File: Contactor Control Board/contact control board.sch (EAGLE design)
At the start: 36 parts, among them Q1 2n2222, Q2 2n2222, Q3 2n2222, Q4 MOSFET-NCHANNELFQP30N06L

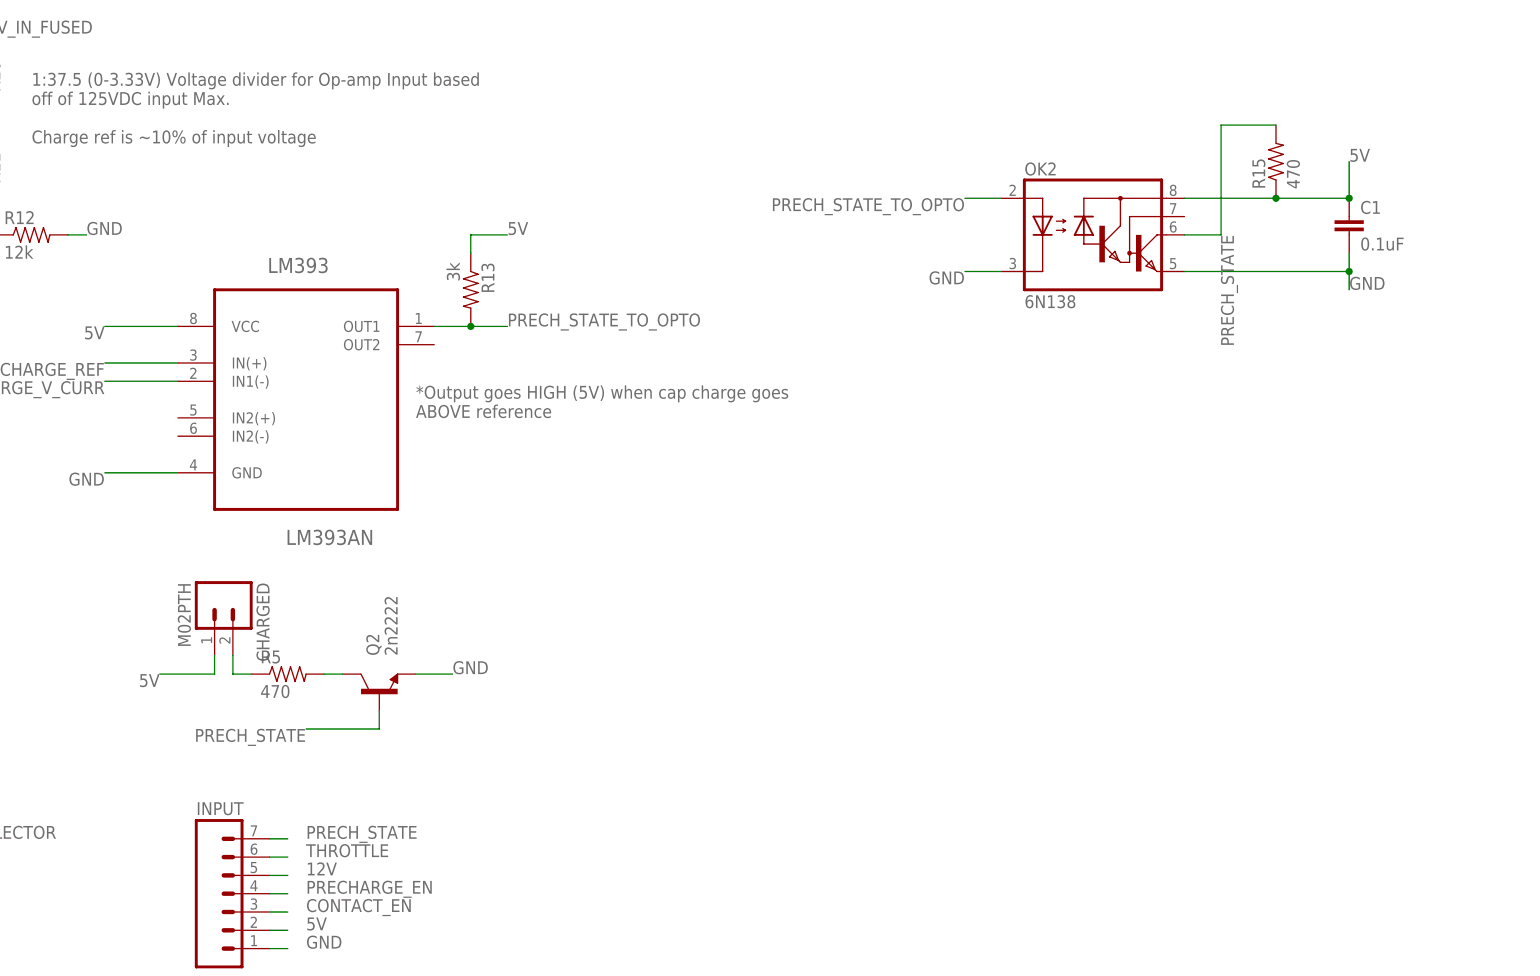
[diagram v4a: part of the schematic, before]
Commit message: Added buffer to use the output of the Op-Amp and split
it between an indicator LED and a digital signal output. Tested and
validated using breadboards
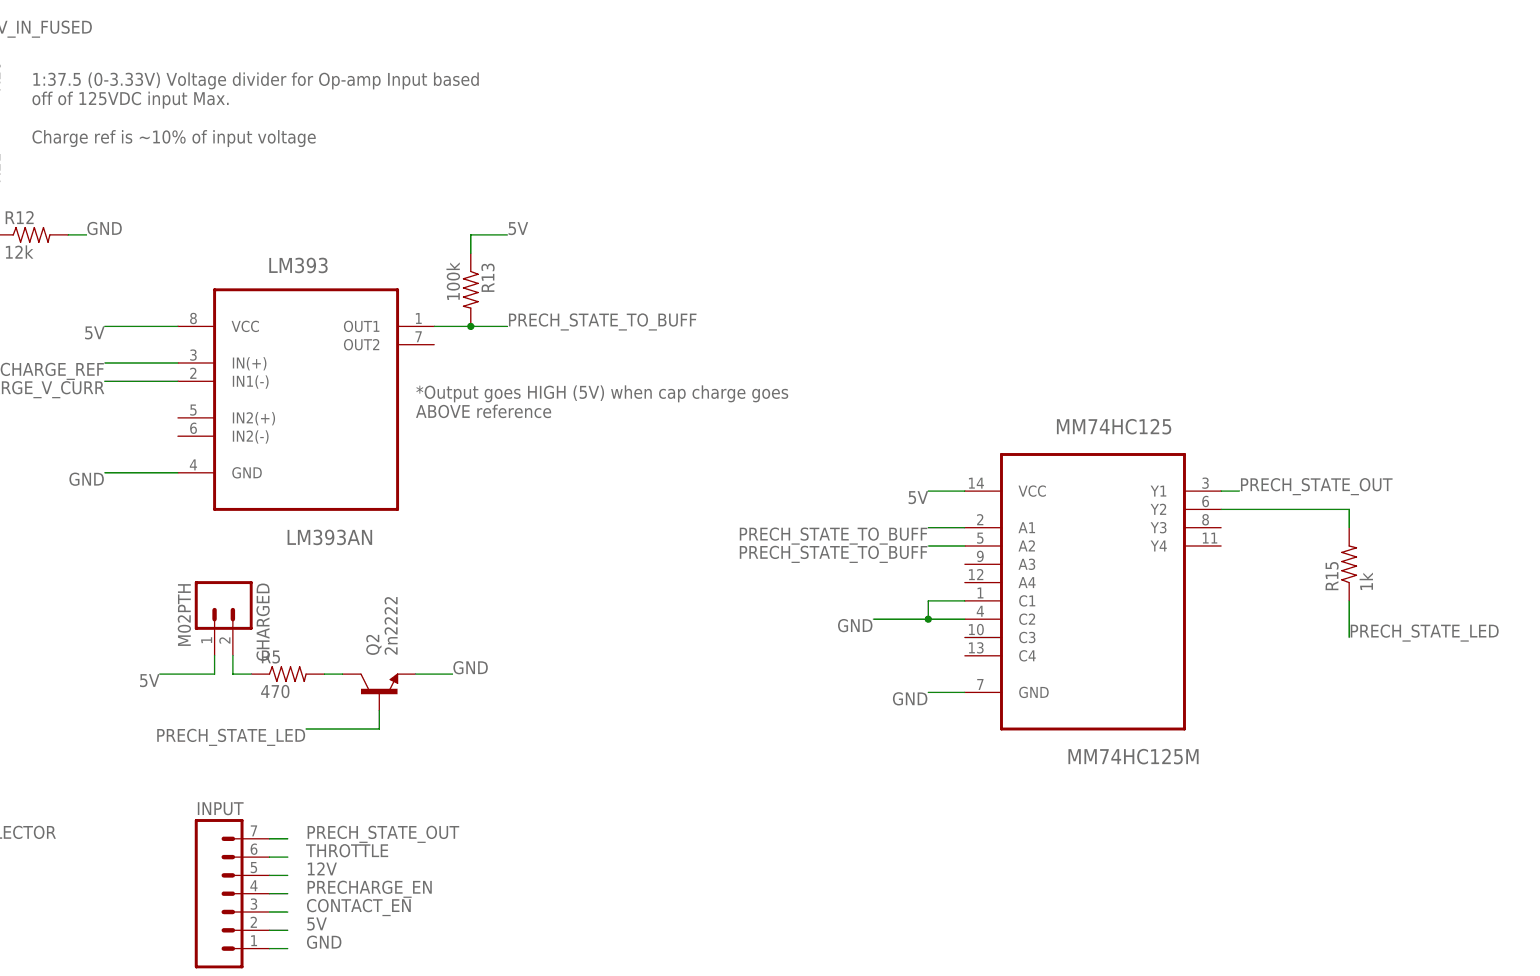
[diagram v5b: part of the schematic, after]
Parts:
- removed C1: 0.1uF, SparkFun-Capacitors:CAP0603-CAP
- removed OK2: 6N138, optocoupler:6N138
- added MM74HC125: MM74HC125M, Fairchild_By_element14_Batch_1:MM74HC125M
- R13: value 3k -> 100k
- R15: value 470 -> 1k
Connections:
- removed net PRECH_STATE: INPUT.7, OK2.VO, Q2.B, R15.2
- removed net PRECH_STATE_TO_OPTO: LM393.OUT1, OK2.A, R13.2
- new net N$6: MM74HC125.Y2, R15.2
- new net PRECH_STATE_LED: Q2.B, R15.1
- new net PRECH_STATE_OUT: INPUT.7, MM74HC125.Y1
- new net PRECH_STATE_TO_BUFF: LM393.OUT1, MM74HC125.A1, MM74HC125.A2, R13.2
- net 5V: now also MM74HC125.VCC; no longer C1.1, OK2.VCC, R15.1
- net GND: now also MM74HC125.C1, MM74HC125.C2, MM74HC125.GND; no longer C1.2, OK2.C, OK2.GND
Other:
- moved on the sheet: R15
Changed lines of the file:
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@@
 <?xml version="1.0" encoding="utf-8"?>
 <!DOCTYPE eagle SYSTEM "eagle.dtd">
-<eagle version="6.4">
+<eagle version="6.5.0">
 <drawing>
 <settings>
@@
 <part name="R11" library="SparkFun-Resistors" deviceset="RESISTOR" device="PTH-1/4W" value="110k"/>
 <part name="R12" library="SparkFun-Resistors" deviceset="RESISTOR" device="PTH-1/4W" value="12k"/>
-<part name="R13" library="SparkFun-Resistors" deviceset="RESISTOR" device="PTH-1/4W" value="3k"/>
+<part name="R13" library="SparkFun-Resistors" deviceset="RESISTOR" device="PTH-1/4W" value="100k"/>
 <part name="PRECHARGE_RELAY" library="relay" deviceset="DS2Y-S-DC*" device="" technology="5V"/>
 <part name="LM393" library="Fairchild_By_element14_Batch_1" deviceset="LM393AN" device=""/>
@@
 <part name="R5" library="SparkFun-Resistors" deviceset="RESISTOR" device="PTH-1/4W" value="470"/>
 <part name="R14" library="SparkFun-Resistors" deviceset="RESISTOR" device="PTH-1/4W" value="10K"/>
-<part name="C1" library="SparkFun-Capacitors" deviceset="CAP" device="0603-CAP" value="0.1uF"/>
-<part name="R15" library="SparkFun-Resistors" deviceset="RESISTOR" device="PTH-1/4W" value="470"/>
-<part name="OK2" library="optocoupler" deviceset="6N138" device=""/>
+<part name="MM74HC125" library="Fairchild_By_element14_Batch_1" deviceset="MM74HC125M" device=""/>
+<part name="R15" library="SparkFun-Resistors" deviceset="RESISTOR" device="PTH-1/4W" value="1k"/>
 </parts>
 <sheets>
@@
 <instance part="R5" gate="G$1" x="129.54" y="78.74"/>
 <instance part="R14" gate="G$1" x="20.32" y="38.1" rot="R180"/>
-<instance part="C1" gate="G$1" x="276.86" y="139.7"/>
-<instance part="R15" gate="G$1" x="266.7" y="149.86" rot="R90"/>
-<instance part="OK2" gate="G$1" x="241.3" y="139.7"/>
+<instance part="MM74HC125" gate="A" x="241.3" y="93.98"/>
+<instance part="R15" gate="G$1" x="276.86" y="93.98" rot="R90"/>
 </instances>
 <busses>
@@
 </segment>
 <segment>
-<pinref part="C1" gate="G$1" pin="1"/>
-<wire x1="254" y1="144.78" x2="266.7" y2="144.78" width="0.2032" layer="91"/>
-<junction x="276.86" y="144.78"/>
-<wire x1="266.7" y1="144.78" x2="276.86" y2="144.78" width="0.2032" layer="91"/>
-<wire x1="276.86" y1="144.78" x2="276.86" y2="149.86" width="0.2032" layer="91"/>
-<pinref part="R15" gate="G$1" pin="1"/>
-<junction x="266.7" y="144.78"/>
-<pinref part="OK2" gate="G$1" pin="VCC"/>
-<label x="276.86" y="149.86" size="1.778" layer="95"/>
+<pinref part="MM74HC125" gate="A" pin="VCC"/>
+<wire x1="223.52" y1="104.14" x2="218.44" y2="104.14" width="0.2032" layer="91"/>
+<label x="218.44" y="104.14" size="1.778" layer="95" rot="R180"/>
 </segment>
 </net>
@@
 </segment>
 <segment>
-<pinref part="OK2" gate="G$1" pin="C"/>
-<wire x1="228.6" y1="134.62" x2="223.52" y2="134.62" width="0.2032" layer="91"/>
-<label x="223.52" y="134.62" size="1.778" layer="95" rot="R180"/>
-</segment>
-<segment>
-<pinref part="C1" gate="G$1" pin="2"/>
-<wire x1="276.86" y1="137.16" x2="276.86" y2="134.62" width="0.2032" layer="91"/>
-<pinref part="OK2" gate="G$1" pin="GND"/>
-<wire x1="276.86" y1="134.62" x2="276.86" y2="132.08" width="0.2032" layer="91"/>
-<wire x1="254" y1="134.62" x2="276.86" y2="134.62" width="0.2032" layer="91"/>
-<junction x="276.86" y="134.62"/>
-<label x="276.86" y="132.08" size="1.778" layer="95"/>
+<pinref part="MM74HC125" gate="A" pin="GND"/>
+<wire x1="223.52" y1="76.2" x2="218.44" y2="76.2" width="0.2032" layer="91"/>
+<label x="218.44" y="76.2" size="1.778" layer="95" rot="R180"/>
+</segment>
+<segment>
+<pinref part="MM74HC125" gate="A" pin="C1"/>
+<wire x1="223.52" y1="88.9" x2="218.44" y2="88.9" width="0.2032" layer="91"/>
+<wire x1="218.44" y1="88.9" x2="218.44" y2="86.36" width="0.2032" layer="91"/>
+<wire x1="218.44" y1="86.36" x2="210.82" y2="86.36" width="0.2032" layer="91"/>
+<pinref part="MM74HC125" gate="A" pin="C2"/>
+<wire x1="223.52" y1="86.36" x2="218.44" y2="86.36" width="0.2032" layer="91"/>
+<junction x="218.44" y="86.36"/>
+<label x="210.82" y="86.36" size="1.778" layer="95" rot="R180"/>
 </segment>
 </net>
@@
 </segment>
 </net>
-<net name="PRECH_STATE" class="0">
+<net name="PRECH_STATE_OUT" class="0">
 <segment>
 <wire x1="127" y1="55.88" x2="129.54" y2="55.88" width="0.2032" layer="91"/>
@@
 </segment>
 <segment>
-<pinref part="Q2" gate="G$1" pin="B"/>
-<wire x1="142.24" y1="73.66" x2="142.24" y2="71.12" width="0.2032" layer="91"/>
-<wire x1="142.24" y1="71.12" x2="132.08" y2="71.12" width="0.2032" layer="91"/>
-<label x="132.08" y="71.12" size="1.778" layer="95" rot="R180"/>
-</segment>
-<segment>
-<pinref part="R15" gate="G$1" pin="2"/>
-<wire x1="266.7" y1="154.94" x2="259.08" y2="154.94" width="0.2032" layer="91"/>
-<wire x1="259.08" y1="154.94" x2="259.08" y2="139.7" width="0.2032" layer="91"/>
-<pinref part="OK2" gate="G$1" pin="VO"/>
-<wire x1="259.08" y1="139.7" x2="254" y2="139.7" width="0.2032" layer="91"/>
-<label x="259.08" y="139.7" size="1.778" layer="95" rot="R270"/>
+<pinref part="MM74HC125" gate="A" pin="Y1"/>
+<wire x1="259.08" y1="104.14" x2="261.62" y2="104.14" width="0.2032" layer="91"/>
+<label x="261.62" y="104.14" size="1.778" layer="95"/>
 </segment>
 </net>
@@
 </segment>
 </net>
-<net name="PRECH_STATE_TO_OPTO" class="0">
+<net name="PRECH_STATE_TO_BUFF" class="0">
 <segment>
 <label x="160.02" y="127" size="1.778" layer="95"/>
@@
 </segment>
 <segment>
-<pinref part="OK2" gate="G$1" pin="A"/>
-<wire x1="228.6" y1="144.78" x2="223.52" y2="144.78" width="0.2032" layer="91"/>
-<label x="223.52" y="144.78" size="1.778" layer="95" rot="R180"/>
-</segment>
-</net>
+<pinref part="MM74HC125" gate="A" pin="A1"/>
+<wire x1="223.52" y1="99.06" x2="218.44" y2="99.06" width="0.2032" layer="91"/>
+<label x="218.44" y="99.06" size="1.778" layer="95" rot="R180"/>
+</segment>
+<segment>
+<pinref part="MM74HC125" gate="A" pin="A2"/>
+<wire x1="223.52" y1="96.52" x2="218.44" y2="96.52" width="0.2032" layer="91"/>
+<label x="218.44" y="96.52" size="1.778" layer="95" rot="R180"/>
+</segment>
+</net>
+<net name="PRECH_STATE_LED" class="0">
+<segment>
+<pinref part="Q2" gate="G$1" pin="B"/>
+<wire x1="142.24" y1="73.66" x2="142.24" y2="71.12" width="0.2032" layer="91"/>
+<wire x1="142.24" y1="71.12" x2="132.08" y2="71.12" width="0.2032" layer="91"/>
+<label x="132.08" y="71.12" size="1.778" layer="95" rot="R180"/>
+</segment>
+<segment>
+<pinref part="R15" gate="G$1" pin="1"/>
+<wire x1="276.86" y1="88.9" x2="276.86" y2="83.82" width="0.2032" layer="91"/>
+<label x="276.86" y="83.82" size="1.778" layer="95"/>
+</segment>
+</net>
+<net name="N$6" class="0">
+<segment>
+<pinref part="MM74HC125" gate="A" pin="Y2"/>
+<pinref part="R15" gate="G$1" pin="2"/>
+<wire x1="259.08" y1="101.6" x2="276.86" y2="101.6" width="0.2032" layer="91"/>
+<wire x1="276.86" y1="101.6" x2="276.86" y2="99.06" width="0.2032" layer="91"/>
+</segment>
+</net>
